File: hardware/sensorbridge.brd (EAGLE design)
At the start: 52.1 x 53.3 mm, 23 parts

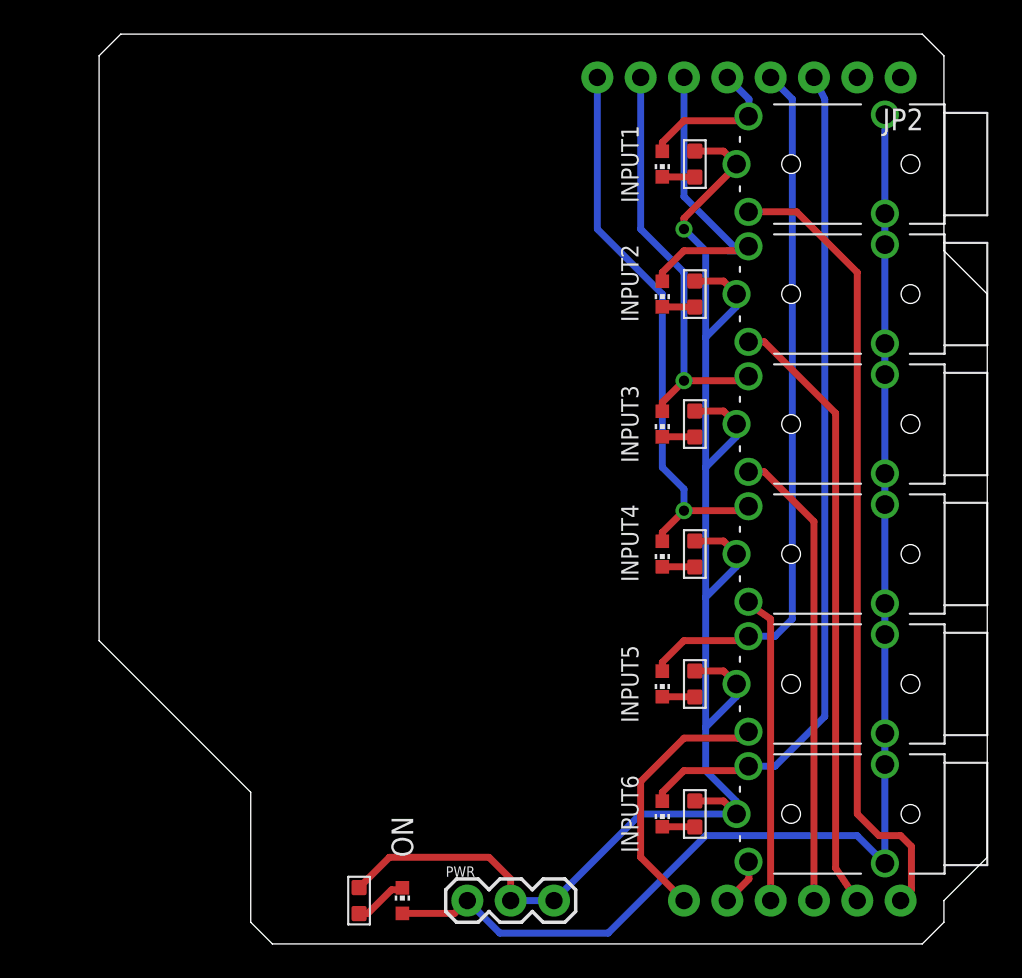
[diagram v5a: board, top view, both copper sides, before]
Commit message: Tweaked board dimensions
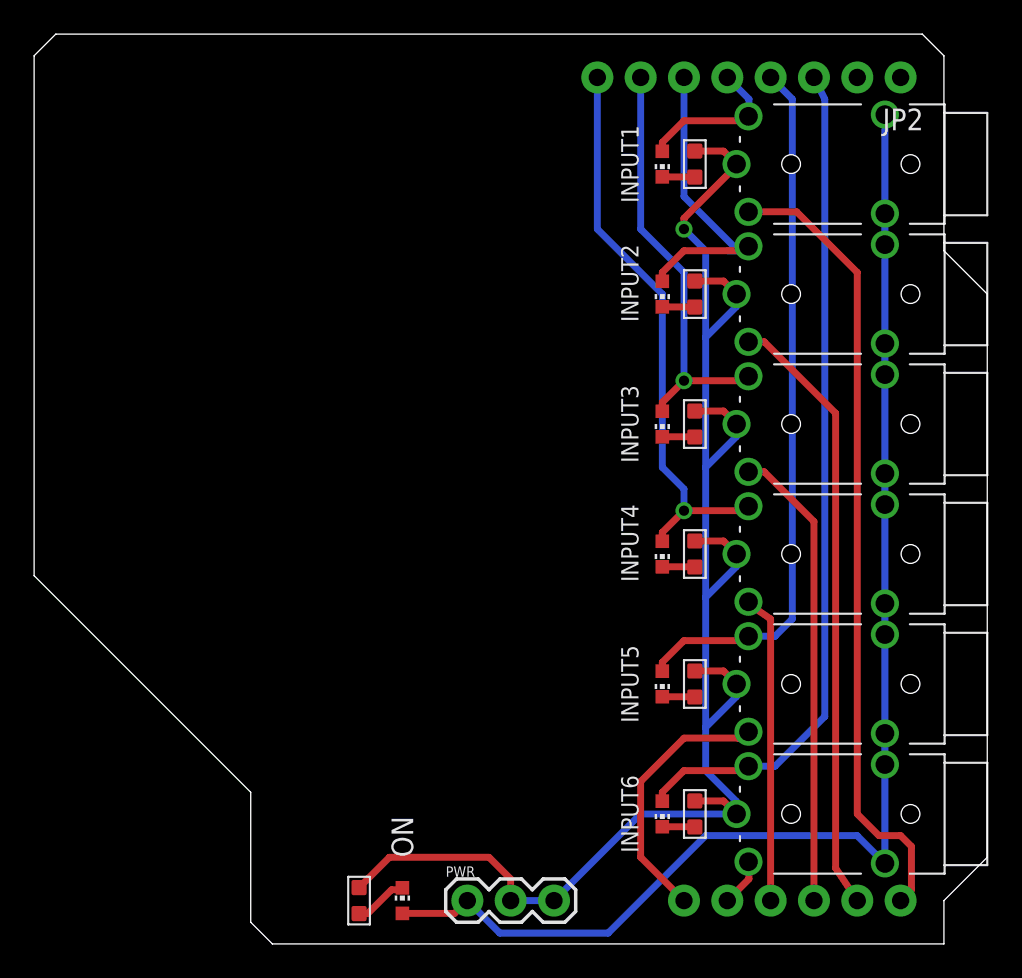
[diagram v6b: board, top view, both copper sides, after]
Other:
- board size 52.1 x 53.3 mm -> 55.9 x 53.3 mm
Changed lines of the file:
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@@
 <?xml version="1.0" encoding="utf-8"?>
 <!DOCTYPE eagle SYSTEM "eagle.dtd">
-<eagle version="7.7.0">
+<eagle version="8.0.0">
 <drawing>
 <settings>
@@
 <setting verticaltext="up"/>
 </settings>
-<grid distance="0.05" unitdist="inch" unit="inch" style="lines" multiple="1" display="yes" altdistance="0.025" altunitdist="inch" altunit="inch"/>
+<grid distance="0.05" unitdist="inch" unit="mm" style="lines" multiple="1" display="yes" altdistance="0.025" altunitdist="inch" altunit="inch"/>
 <layers>
 <layer number="1" name="Top" color="4" fill="1" visible="yes" active="yes"/>
@@
 <board>
 <plain>
-<wire x1="26.67" y1="0" x2="64.77" y2="0" width="0" layer="20"/>
-<wire x1="64.77" y1="0" x2="66.04" y2="1.27" width="0" layer="20"/>
-<wire x1="66.04" y1="1.27" x2="66.04" y2="2.54" width="0" layer="20"/>
+<wire x1="26.67" y1="0" x2="66.04" y2="0" width="0" layer="20"/>
+<wire x1="66.04" y1="0" x2="66.04" y2="2.54" width="0" layer="20"/>
 <wire x1="66.04" y1="2.54" x2="68.58" y2="5.08" width="0" layer="20"/>
 <wire x1="68.58" y1="5.08" x2="68.58" y2="38.1" width="0" layer="20"/>
@@
 <wire x1="66.04" y1="40.64" x2="66.04" y2="52.07" width="0" layer="20"/>
 <wire x1="66.04" y1="52.07" x2="64.77" y2="53.34" width="0" layer="20"/>
-<wire x1="64.77" y1="53.34" x2="17.78" y2="53.34" width="0" layer="20"/>
-<wire x1="17.78" y1="53.34" x2="16.51" y2="52.07" width="0" layer="20"/>
-<wire x1="16.51" y1="52.07" x2="16.51" y2="17.78" width="0" layer="20"/>
-<wire x1="16.51" y1="17.78" x2="25.4" y2="8.89" width="0" layer="20"/>
+<wire x1="64.77" y1="53.34" x2="13.97" y2="53.34" width="0" layer="20"/>
+<wire x1="13.97" y1="53.34" x2="12.7" y2="52.07" width="0" layer="20"/>
+<wire x1="12.7" y1="52.07" x2="12.7" y2="21.59" width="0" layer="20"/>
+<wire x1="12.7" y1="21.59" x2="25.4" y2="8.89" width="0" layer="20"/>
 <wire x1="25.4" y1="8.89" x2="25.4" y2="1.27" width="0" layer="20"/>
 <wire x1="25.4" y1="1.27" x2="26.67" y2="0" width="0" layer="20"/>
@@
 <wire x1="54.32" y1="33.02" x2="54.58" y2="33.28" width="0.4064" layer="1"/>
 <contactref element="JP2" pad="7"/>
-<via x="50.8" y="33.02" extent="1-16" drill="0.6" shape="square"/>
+<via x="50.8" y="33.02" extent="1-16" drill="0.6"/>
 <wire x1="50.8" y1="33.02" x2="50.8" y2="39.37" width="0.4064" layer="16"/>
 <wire x1="50.8" y1="39.37" x2="48.26" y2="41.91" width="0.4064" layer="16"/>
@@
 <wire x1="54.32" y1="25.4" x2="54.58" y2="25.66" width="0.4064" layer="1"/>
 <contactref element="JP2" pad="8"/>
-<via x="50.8" y="25.4" extent="1-16" drill="0.6" shape="square"/>
+<via x="50.8" y="25.4" extent="1-16" drill="0.6"/>
 <wire x1="50.8" y1="25.4" x2="50.8" y2="26.67" width="0.4064" layer="16"/>
 <wire x1="50.8" y1="26.67" x2="49.53" y2="27.94" width="0.4064" layer="16"/>

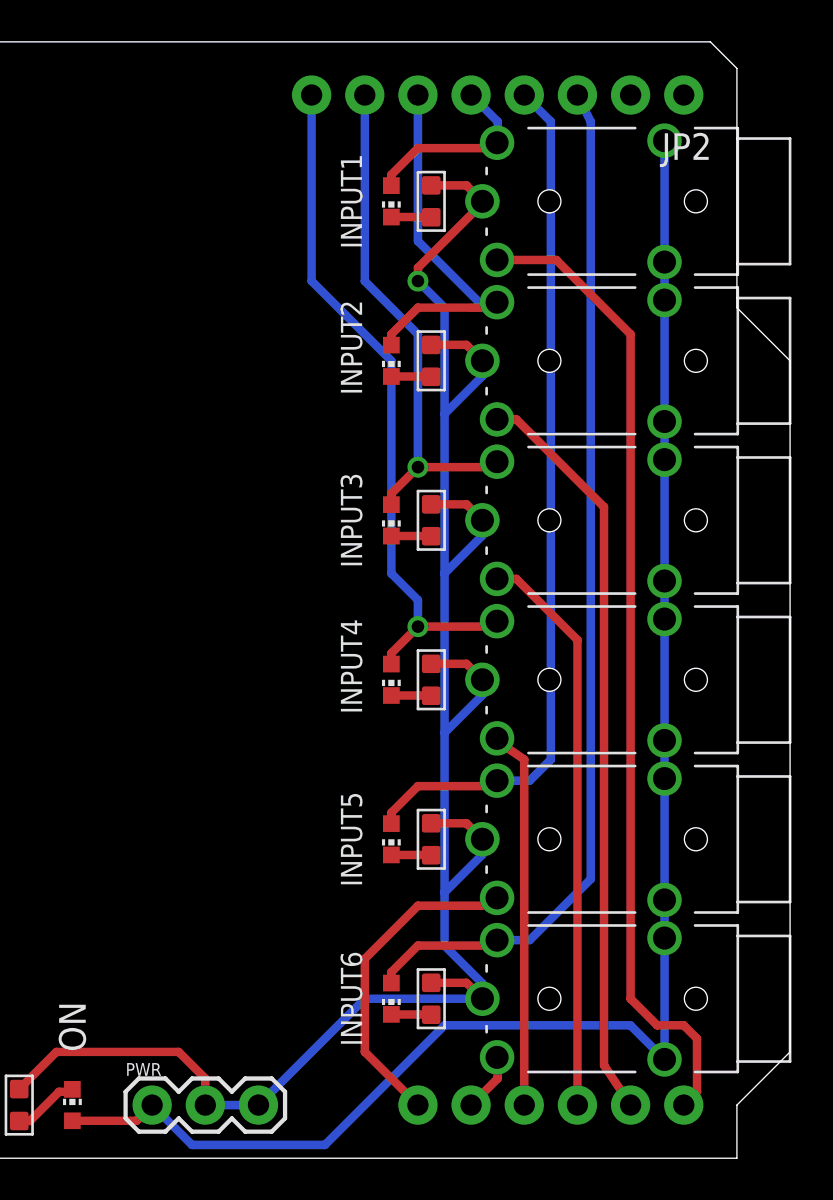
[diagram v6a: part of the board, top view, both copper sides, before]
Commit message: Replaced header parts for headers with silkscreen
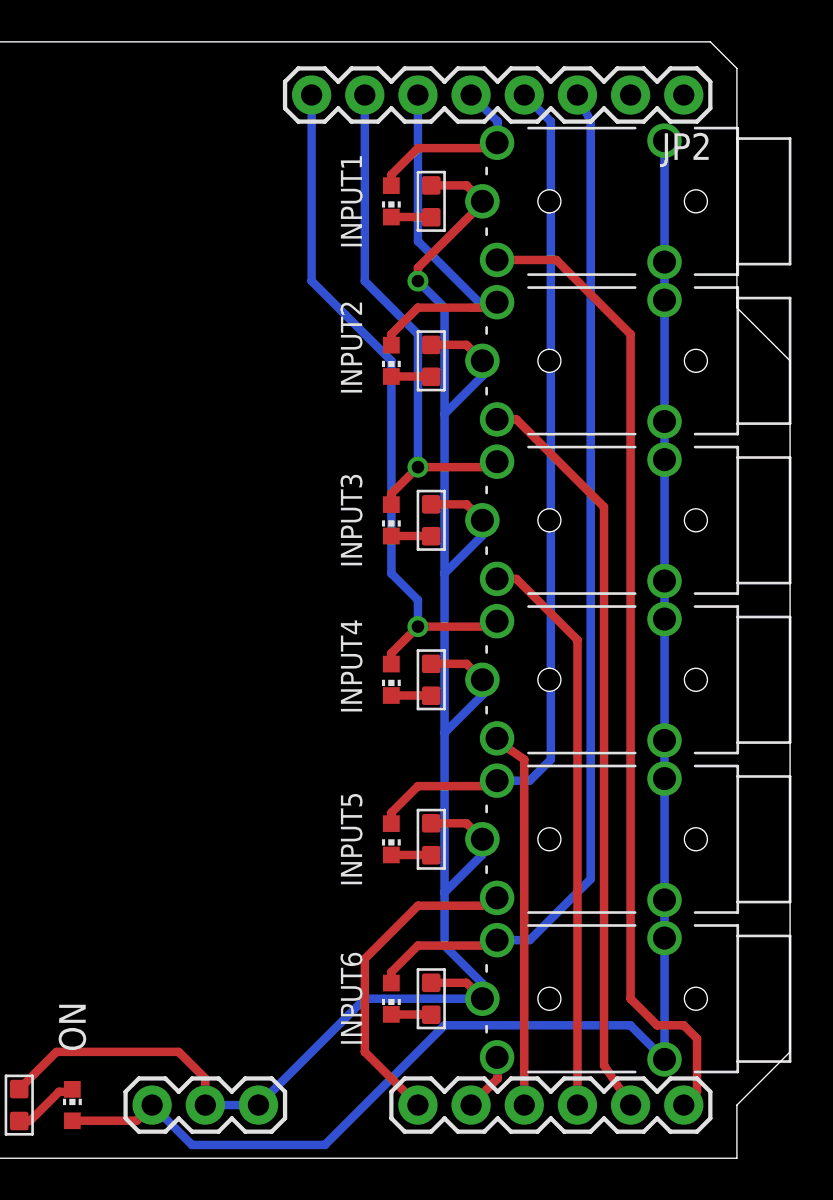
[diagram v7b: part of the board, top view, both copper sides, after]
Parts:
- ANALOG: device SparkFun-Connectors:1X06_NO_SILK -> SparkFun-Connectors:1X06
- JP2: device SparkFun-Connectors:1X08_NO_SILK -> SparkFun-Connectors:1X08_ROUND
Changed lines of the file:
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@@
 <attribute name="NAME" x="47.625" y="7.62" size="1.016" layer="21" rot="R270" align="center"/>
 </element>
-<element name="ANALOG" library="SparkFun-Connectors" package="1X06_NO_SILK" value="" x="50.8" y="2.54" smashed="yes">
+<element name="ANALOG" library="SparkFun-Connectors" package="1X06" value="" x="50.8" y="2.54" smashed="yes">
 <attribute name="PROD_ID" value="CONN-08437" x="50.8" y="2.54" size="1.778" layer="27" display="off"/>
 <attribute name="VALUE" x="49.53" y="-0.635" size="1.27" layer="27"/>
 </element>
-<element name="JP2" library="SparkFun-Connectors" package="1X08_NO_SILK" value="" x="63.5" y="50.8" rot="R180">
-<attribute name="PROD_ID" value="CONN-08438" x="63.5" y="50.8" size="1.778" layer="27" rot="R180" display="off"/>
-</element>
+<element name="JP2" library="SparkFun-Connectors" package="1X08_ROUND" value="" x="63.5" y="50.8" rot="R180"/>
 <element name="ON" library="adafruit" package="CHIP-LED0603" value="" x="34.29" y="2.54" smashed="yes">
 <attribute name="NAME" x="34.29" y="5.08" size="1.27" layer="25" rot="R270" align="center-right"/>
@@
 <attribute name="VALUE" x="33.655" y="1.27" size="0.635" layer="27" ratio="10" rot="R90"/>
 </element>
-<element name="PWR" library="SparkFun-Connectors" package="1X03" value="" x="38.1" y="2.54"/>
+<element name="PWR" library="SparkFun-Connectors" package="1X03" value="" x="38.1" y="2.54" smashed="yes">
+<attribute name="VALUE" x="36.83" y="0.508" size="0.6096" layer="27" font="vector" ratio="20"/>
+</element>
 </elements>
 <signals>

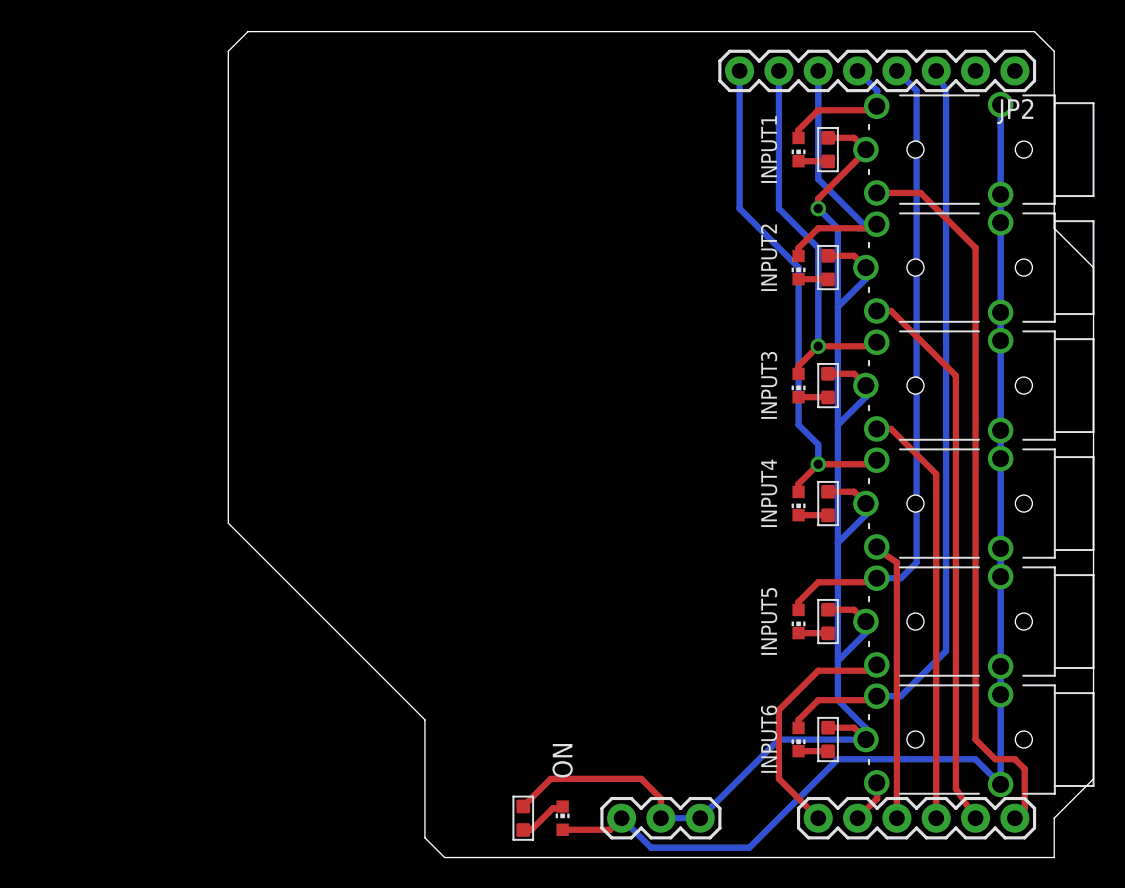
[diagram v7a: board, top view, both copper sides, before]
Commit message: Added top and bottom silks
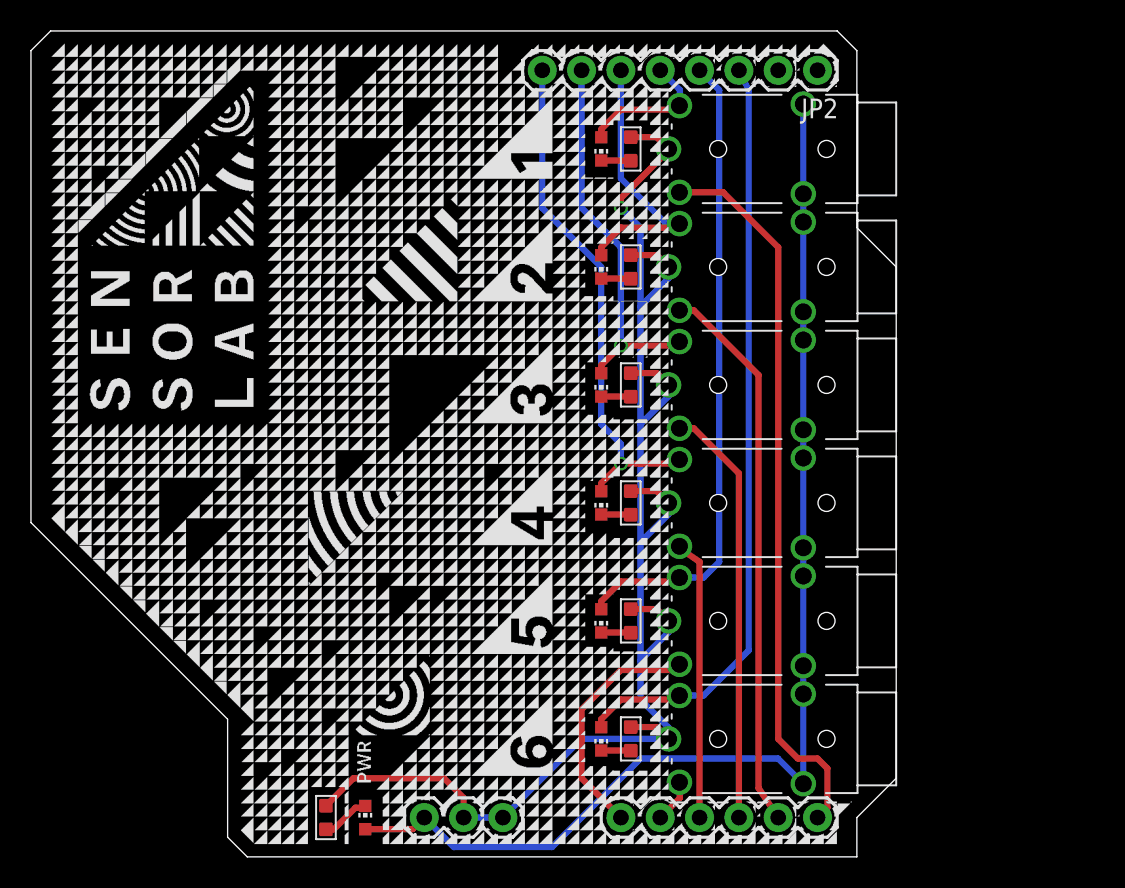
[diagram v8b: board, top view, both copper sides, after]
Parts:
- moved PWR 12.7 mm to (25.4, 2.58)
- moved ANALOG 12.7 mm to (38.1, 2.58)
- moved INPUT1 12.7 mm to (46.9, 45.8)
- moved INPUT2 12.7 mm to (46.9, 38.1)
- moved INPUT3 12.7 mm to (46.9, 30.5)
- moved INPUT4 12.7 mm to (46.9, 22.9)
- moved INPUT5 12.7 mm to (46.9, 15.3)
- moved INPUT6 12.7 mm to (46.9, 7.66)
- moved JP2 12.7 mm to (50.8, 50.8)
- moved LED1 12.7 mm to (36.8, 45.8)
- moved LED2 12.7 mm to (36.8, 38.1)
- moved LED3 12.7 mm to (36.8, 30.5)
- moved LED4 12.7 mm to (36.8, 22.9)
- moved LED5 12.7 mm to (36.8, 15.3)
- moved LED6 12.7 mm to (36.8, 7.66)
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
